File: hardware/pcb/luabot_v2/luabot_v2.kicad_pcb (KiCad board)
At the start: 2 copper layers, 60.3 x 29.8 mm, 21 parts, among them CON1 BAT_IN, P2 GND_GPIO, P3 VCC_GPIO, SW1 RESET, U1 ESP-07V2, U2 LM1117

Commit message: avance hadware tarjeta terminada
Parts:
- moved C1 21.0 mm to (41.0, 25.7)
- moved R3 9.94 mm to (41.1, 33.9), turned to 270 degrees
- moved C2 8.95 mm to (35.7, 35.6)
- moved U2 6.38 mm to (36.2, 43.8), turned to 270 degrees
- moved R5 5.50 mm to (45.3, 31.5)
- moved R7 2.05 mm to (67.9, 34.8)
- moved ADC 1.78 mm to (76.2, 38.9)
- moved P2 1.78 mm to (81.3, 38.9)
- moved P3 1.78 mm to (78.7, 38.9)
- moved 3.3V 1.42 mm to (39.2, 49.1), turned to 0 degrees
- moved R6 0.90 mm to (70.7, 45.5)
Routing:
- net GND: track 98.7 -> 155.5 mm, vias 1 -> 2
- net +3.3V: track 60.1 -> 107.9 mm
- net N-0000021: track 15.2 -> 57.7 mm
- net Reset: track 29.8 -> 63.3 mm
- net TX: track 0.00 -> 25.4 mm, vias 0 -> 1
- net +5V: track 10.5 -> 35.2 mm, vias 1 -> 2
- net RX: track 0.00 -> 24.0 mm, vias 0 -> 1
- net +5V_USB: track 0.00 -> 14.6 mm
- net D0: track 25.6 -> 14.5 mm
- net D5: track 23.7 -> 12.9 mm
- net O02: track 15.0 -> 5.60 mm, vias 1 -> 0
- net O15: track 11.3 -> 20.2 mm
- net ADC: track 10.3 -> 16.7 mm
- net FLASH: track 30.6 -> 27.0 mm
- net D2: track 27.6 -> 29.8 mm
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- added copper zone on B.Cu, net GND
- added copper zone on F.Cu, net GND
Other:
- board size 60.3 x 29.8 mm -> 67.8 x 32.1 mm
- board text added: "ADC"
- board text added: "FLASH"
- board text added: "RESET"
- board text added: "VCC"

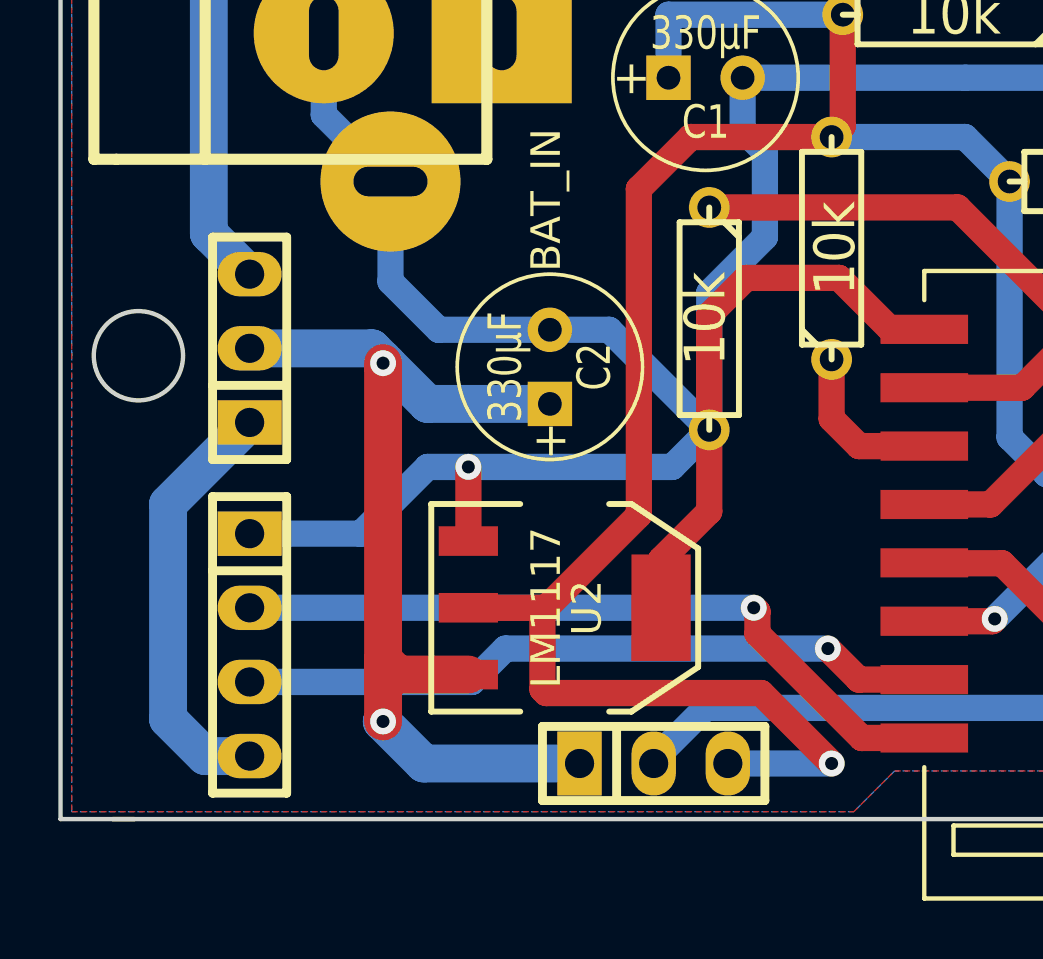
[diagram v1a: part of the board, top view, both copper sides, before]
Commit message: librerias y footprints componentes
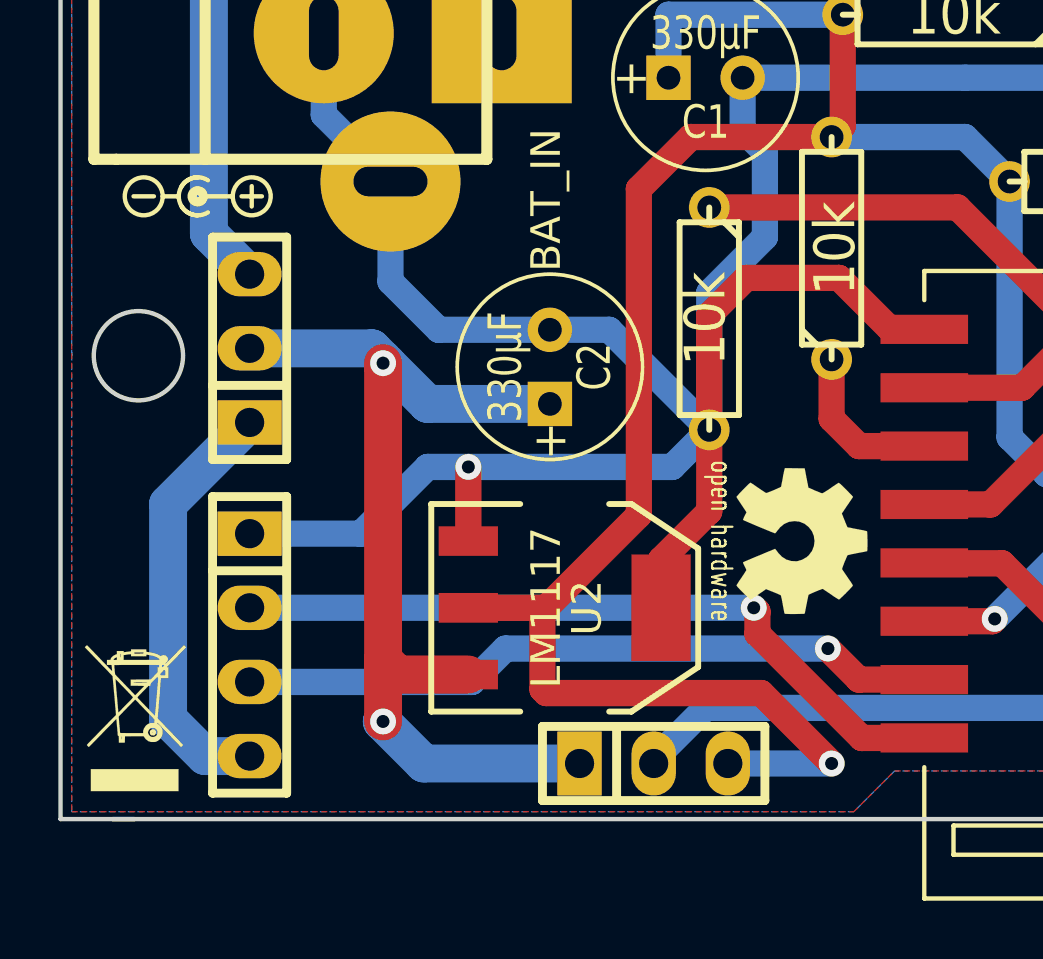
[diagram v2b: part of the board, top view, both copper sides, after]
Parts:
- added G***: LOGO, Logo_silk_polarity_center_5x1.4mm, F.Cu at (23.6, 29.7)
- added G***: LOGO, Logo_silk_WEEE_3.4x5mm, F.Cu at (21.5, 47.6)
- added G***: LOGO, Logo_silk_OSHW_6x6mm, F.Cu at (44.3, 41.5)
